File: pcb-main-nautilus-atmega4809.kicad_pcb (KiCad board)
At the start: 4 copper layers, 68.6 x 53.3 mm, 91 parts, among them J1 694106301002, J2 105017-0001, J3 FTSH-105-01-L-DV-007-K, J4 75844-101-06LF, J5 66951-006LF, J6 66951-010LF, J7 66951-008LF, J8 66951-008LF, Q1 BSS138PW, Q2 BSS138PW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

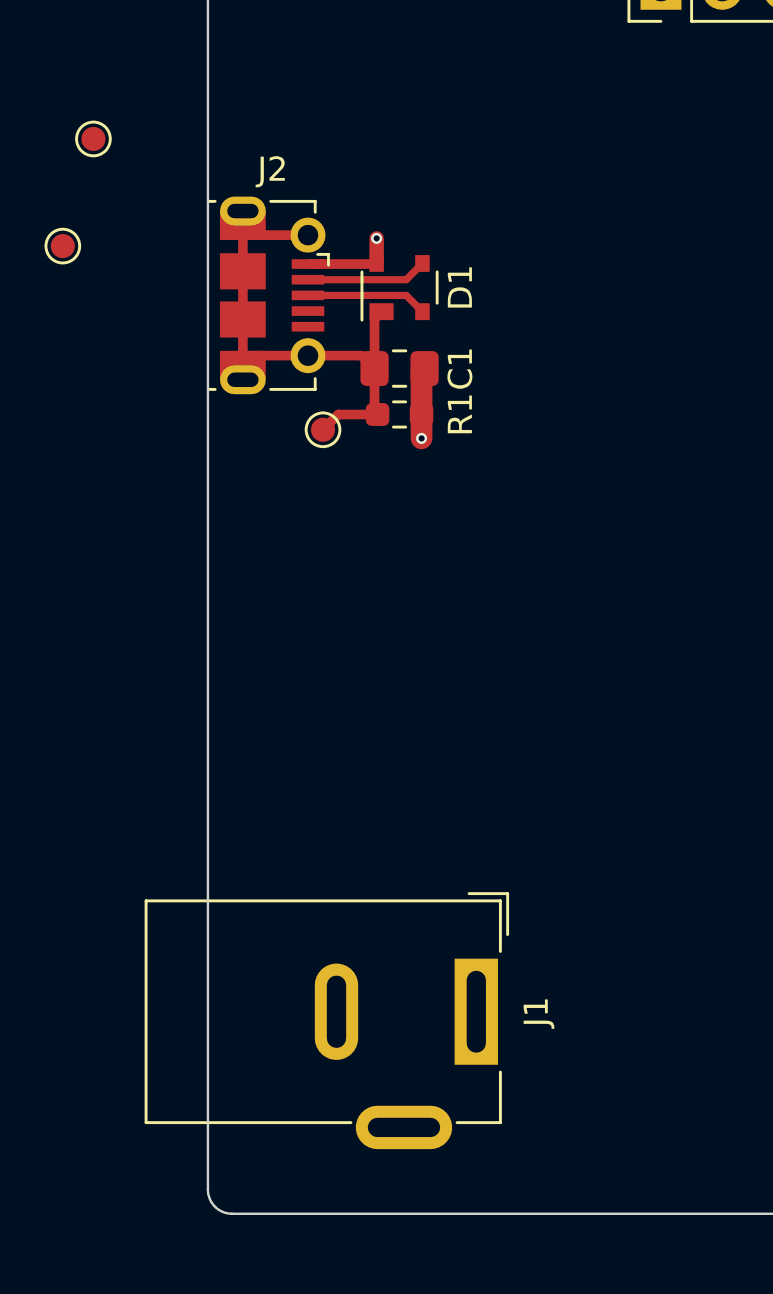
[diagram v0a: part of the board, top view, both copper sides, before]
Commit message: Adjust connector placement to avoid silk DRC errors
Supports #4.
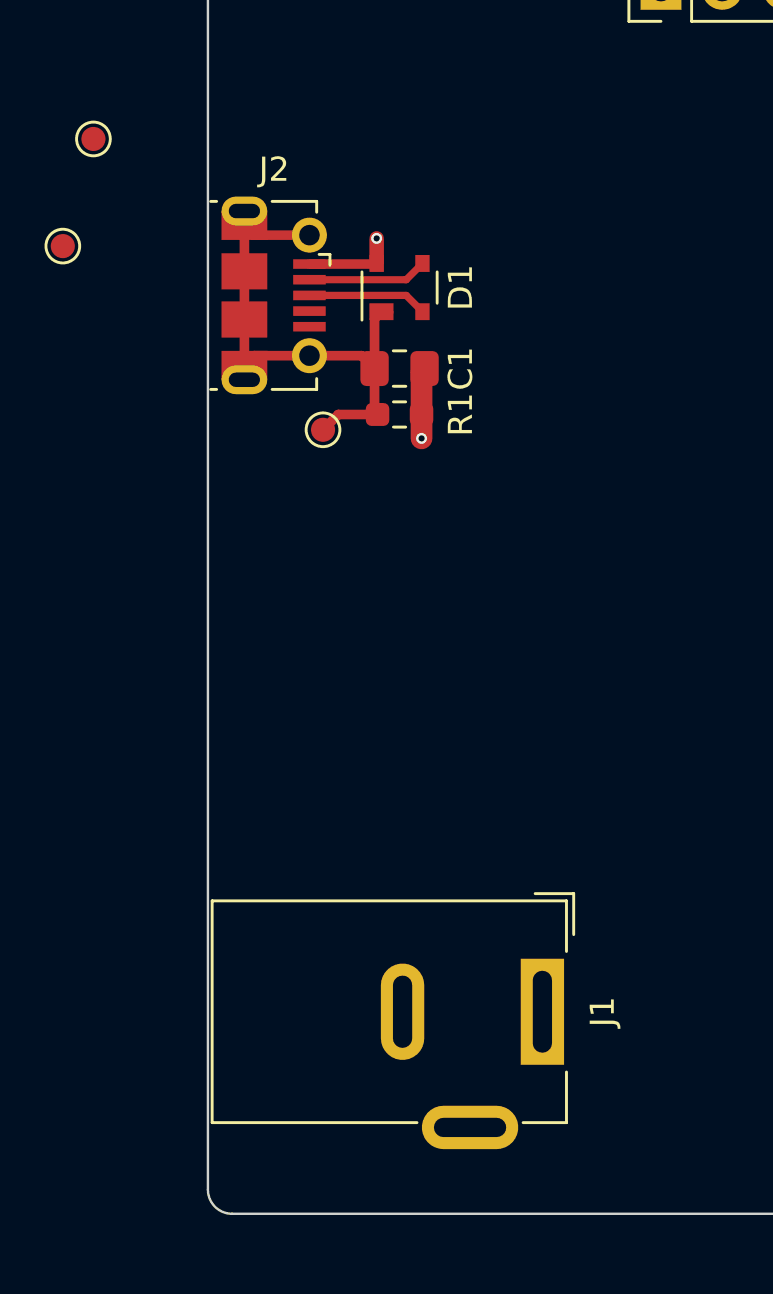
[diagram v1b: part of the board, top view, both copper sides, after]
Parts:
- moved J1 2.74 mm to (113.9, 141.6)
- moved J2 0.06 mm to (102.8, 111.9)
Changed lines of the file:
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@@
   )
   (footprint "Connector_USB:USB_Micro-B_Molex-105017-0001" locked (layer "F.Cu")
-    (at 102.689204 111.9 -90)
+    (at 102.75 111.9 -90)
     (descr "http://www.molex.com/pdm_docs/sd/1050170001_sd.pdf")
     (tags "Micro-USB SMD Typ-B")
@@
   )
   (footprint "Connector_BarrelJack:BarrelJack_Wuerth_6941xx301002" locked (layer "F.Cu")
-    (at 111.134 141.618 -90)
+    (at 113.875 141.618 -90)
     (descr "Wuerth electronics barrel jack connector (5.5mm outher diameter, inner diameter 2.05mm or 2.55mm depending on exact order number), See: http://katalog.we-online.de/em/datasheet/6941xx301002.pdf")
     (tags "connector barrel jack")
@@
   (gr_line locked (start 168.58 144.92) (end 168.58 112.154) (layer "Edge.Cuts") (width 0.1))
   (gr_arc locked (start 100 97.66) (mid 100.292893 96.952893) (end 101 96.66) (layer "Edge.Cuts") (width 0.1))
-  (segment (start 101.851704 109.4) (end 101.451704 109) (width 0.4) (layer "F.Cu") (net 1))
   (segment (start 106.9125 112.8625) (end 107.2 112.575) (width 0.4) (layer "F.Cu") (net 1))
   (segment (start 107.0375 116.84) (end 105.41 116.84) (width 0.4) (layer "F.Cu") (net 1))
-  (segment (start 101.451704 108.4) (end 101.451704 109) (width 0.4) (layer "F.Cu") (net 1))
-  (segment (start 101.451704 114.8) (end 101.451704 115.4) (width 0.4) (layer "F.Cu") (net 1))
-  (segment (start 101.451704 110.9) (end 101.451704 112.9) (width 0.4) (layer "F.Cu") (net 1))
-  (segment (start 104.151704 109.4) (end 101.851704 109.4) (width 0.4) (layer "F.Cu") (net 1))
+  (segment (start 101.5125 108.4) (end 101.5125 109) (width 0.4) (layer "F.Cu") (net 1))
+  (segment (start 101.9125 109.4) (end 101.5125 109) (width 0.4) (layer "F.Cu") (net 1))
+  (segment (start 101.5125 114.8) (end 101.5125 115.4) (width 0.4) (layer "F.Cu") (net 1))
+  (segment (start 101.5125 110.9) (end 101.5125 112.9) (width 0.4) (layer "F.Cu") (net 1))
+  (segment (start 104.2125 114.4) (end 101.9125 114.4) (width 0.4) (layer "F.Cu") (net 1))
   (segment (start 106.9125 116.715) (end 107.0375 116.84) (width 0.4) (layer "F.Cu") (net 1))
   (segment (start 107.635 112.625) (end 107.635 112.575) (width 0.127) (layer "F.Cu") (net 1))
   (segment (start 105.41 116.84) (end 104.775 117.475) (width 0.4) (layer "F.Cu") (net 1))
   (segment (start 106.9125 114.935) (end 106.9125 116.715) (width 0.4) (layer "F.Cu") (net 1))
-  (segment (start 104.151704 114.4) (end 101.851704 114.4) (width 0.4) (layer "F.Cu") (net 1))
+  (segment (start 104.2125 109.4) (end 101.9125 109.4) (width 0.4) (layer "F.Cu") (net 1))
   (segment (start 106.3775 114.4) (end 106.9125 114.935) (width 0.4) (layer "F.Cu") (net 1))
-  (segment (start 101.451704 112.9) (end 101.451704 114.8) (width 0.4) (layer "F.Cu") (net 1))
+  (segment (start 101.5125 112.9) (end 101.5125 114.8) (width 0.4) (layer "F.Cu") (net 1))
   (segment (start 106.9125 114.935) (end 106.9125 112.8625) (width 0.4) (layer "F.Cu") (net 1))
-  (segment (start 104.151704 114.4) (end 106.3775 114.4) (width 0.4) (layer "F.Cu") (net 1))
-  (segment (start 101.851704 114.4) (end 101.451704 114.8) (width 0.4) (layer "F.Cu") (net 1))
-  (segment (start 101.451704 109) (end 101.451704 110.9) (width 0.4) (layer "F.Cu") (net 1))
+  (segment (start 101.5125 109) (end 101.5125 110.9) (width 0.4) (layer "F.Cu") (net 1))
+  (segment (start 104.2125 114.4) (end 106.3775 114.4) (width 0.4) (layer "F.Cu") (net 1))
+  (segment (start 101.9125 114.4) (end 101.5125 114.8) (width 0.4) (layer "F.Cu") (net 1))
   (segment (start 196.6 91.0875) (end 196.6 89.5125) (width 0.3) (layer "F.Cu") (net 2))
   (segment (start 196.6 89.5125) (end 195.9875 88.9) (width 0.3) (layer "F.Cu") (net 2))
@@
   (segment (start 141.605 68.58) (end 141.605 70.485) (width 0.95) (layer "F.Cu") (net 6))
   (segment (start 108.225 111.25) (end 108.9 110.575) (width 0.3) (layer "F.Cu") (net 9))
-  (segment (start 104.151704 111.25) (end 108.225 111.25) (width 0.3) (layer "F.Cu") (net 9))
-  (segment (start 104.151704 111.9) (end 108.225 111.9) (width 0.3) (layer "F.Cu") (net 10))
+  (segment (start 108.225 111.25) (end 104.2125 111.25) (width 0.3) (layer "F.Cu") (net 9))
+  (segment (start 108.225 111.9) (end 104.2125 111.9) (width 0.3) (layer "F.Cu") (net 10))
   (segment (start 108.225 111.9) (end 108.9 112.575) (width 0.3) (layer "F.Cu") (net 10))
-  (segment (start 104.151704 110.6) (end 106.975 110.6) (width 0.4) (layer "F.Cu") (net 11))
   (segment (start 107 110.575) (end 107 109.535) (width 0.6) (layer "F.Cu") (net 11))
   (segment (start 106.975 110.6) (end 107 110.575) (width 0.4) (layer "F.Cu") (net 11))
+  (segment (start 104.2125 110.6) (end 106.975 110.6) (width 0.4) (layer "F.Cu") (net 11))
   (via (at 107 109.535) (size 0.4572) (drill 0.254) (layers "F.Cu" "B.Cu") (net 11))
   (segment (start 65.405 107.315) (end 66.3975 107.315) (width 0.95) (layer "F.Cu") (net 13))

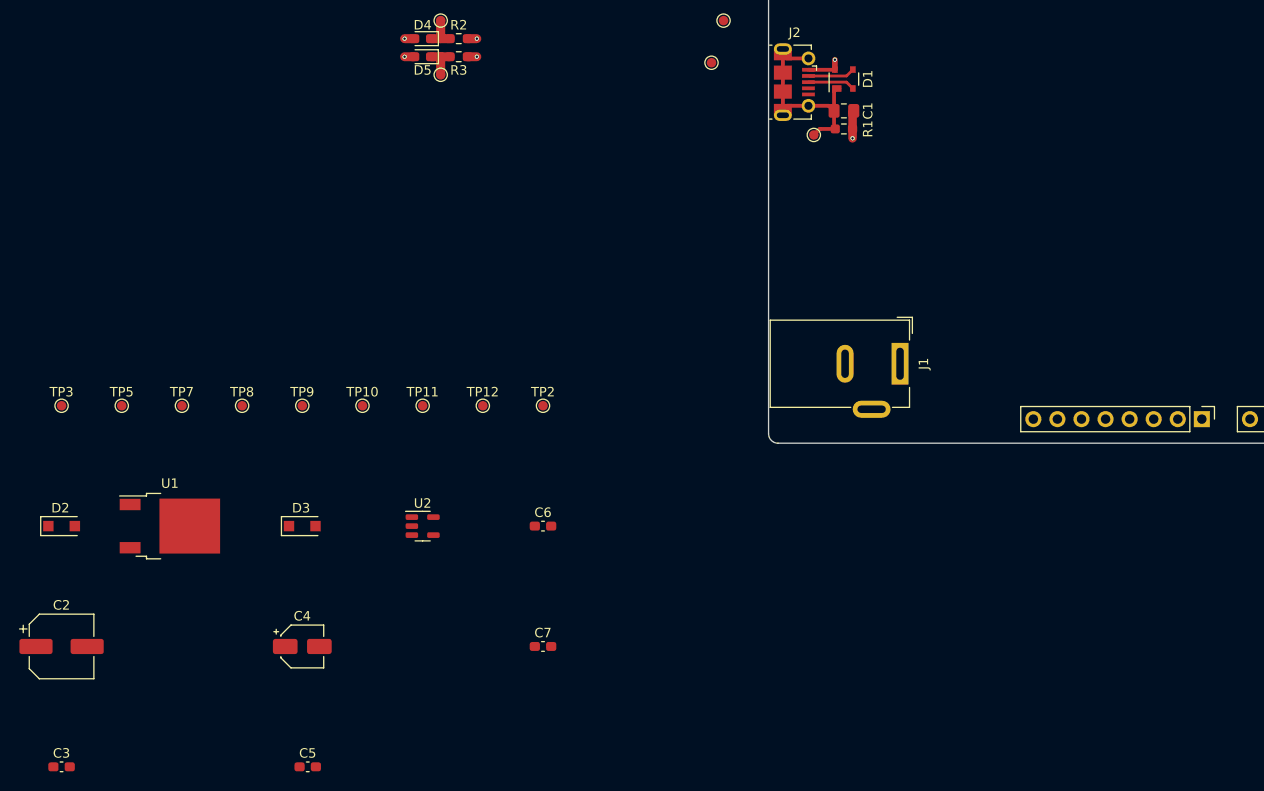
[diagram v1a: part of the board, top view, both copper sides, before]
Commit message: Place 5 V power circuitry
Supports #4.
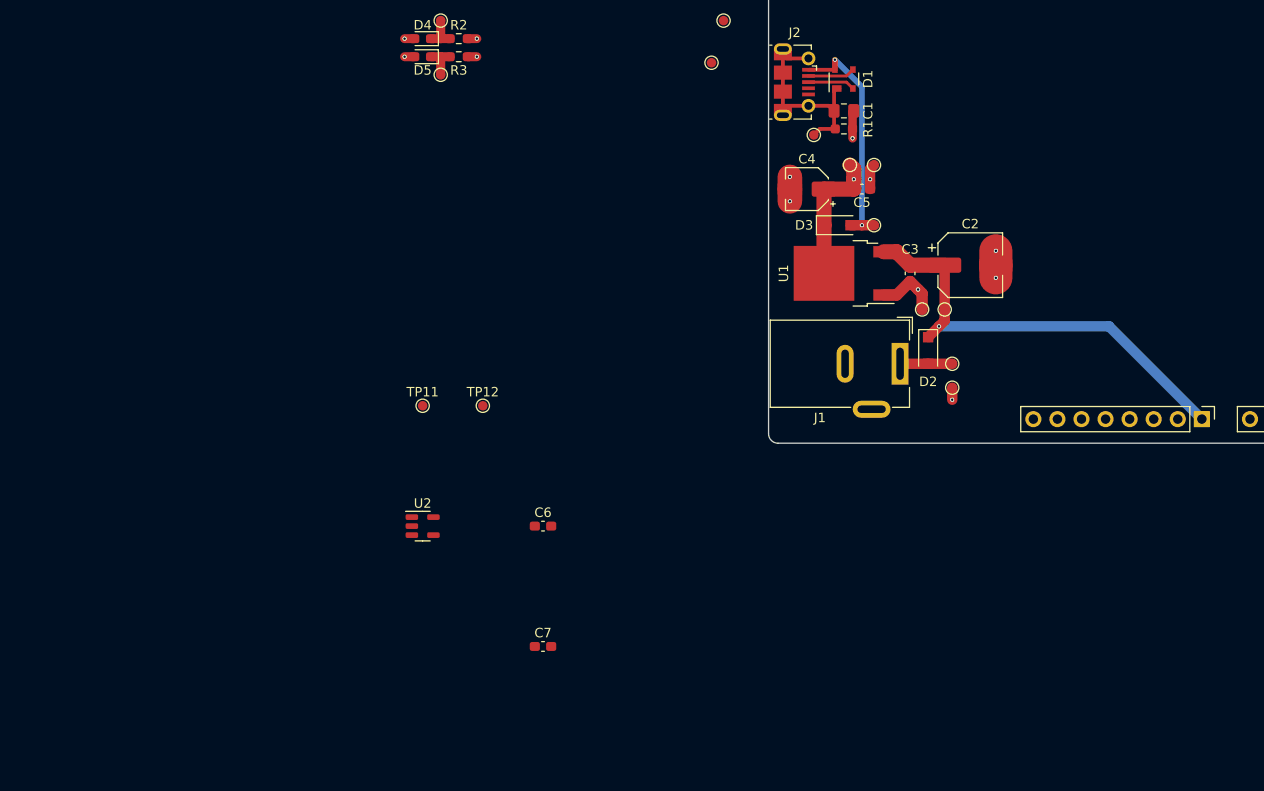
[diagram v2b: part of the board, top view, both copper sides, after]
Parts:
- moved C2 104.0 mm to (121.3, 131.2)
- moved C3 103.6 mm to (114.9, 132.1), turned to -90 degrees
- moved TP3 94.0 mm to (119.4, 144.1)
- moved D2 93.3 mm to (116.8, 140.2), turned to -90 degrees
- moved TP5 87.7 mm to (119.4, 141.6)
- moved C5 84.5 mm to (109.9, 123.2)
- moved TP7 81.1 mm to (118.6, 135.9)
- moved U1 76.0 mm to (108.0, 132.1), turned to 180 degrees
- moved TP8 72.5 mm to (116.2, 135.9)
- moved C4 71.9 mm to (104.0, 123.2), turned to 180 degrees
- moved D3 64.8 mm to (107.2, 127.0)
- moved TP9 63.1 mm to (108.6, 120.7)
- moved TP10 59.7 mm to (111.1, 120.7)
- moved TP2 39.8 mm to (111.1, 127.0)
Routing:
- net /VIN: track 0.00 -> 47.1 mm, vias 0 -> 1
- net /POWER/USB_VBUS: track 3.84 -> 25.0 mm, vias 1 -> 2
- net /GND: track 29.7 -> 45.9 mm, vias 12 -> 19
- net /5V: track 18.9 -> 33.6 mm, vias 10 -> 11
- net /POWER/PWRIN: track 0.00 -> 5.50 mm

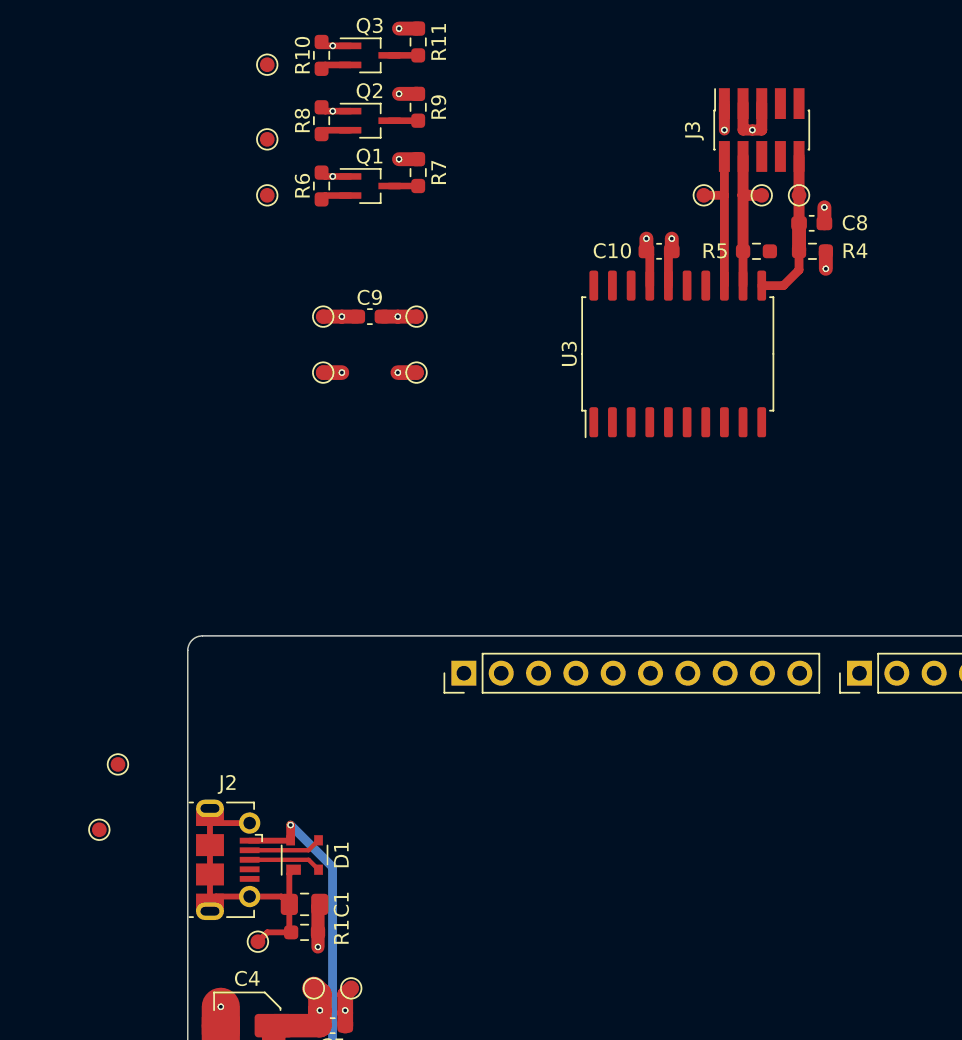
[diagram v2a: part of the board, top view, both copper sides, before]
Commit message: Place UPDI programmer and USB-serial bridge circuitry
Supports #4.
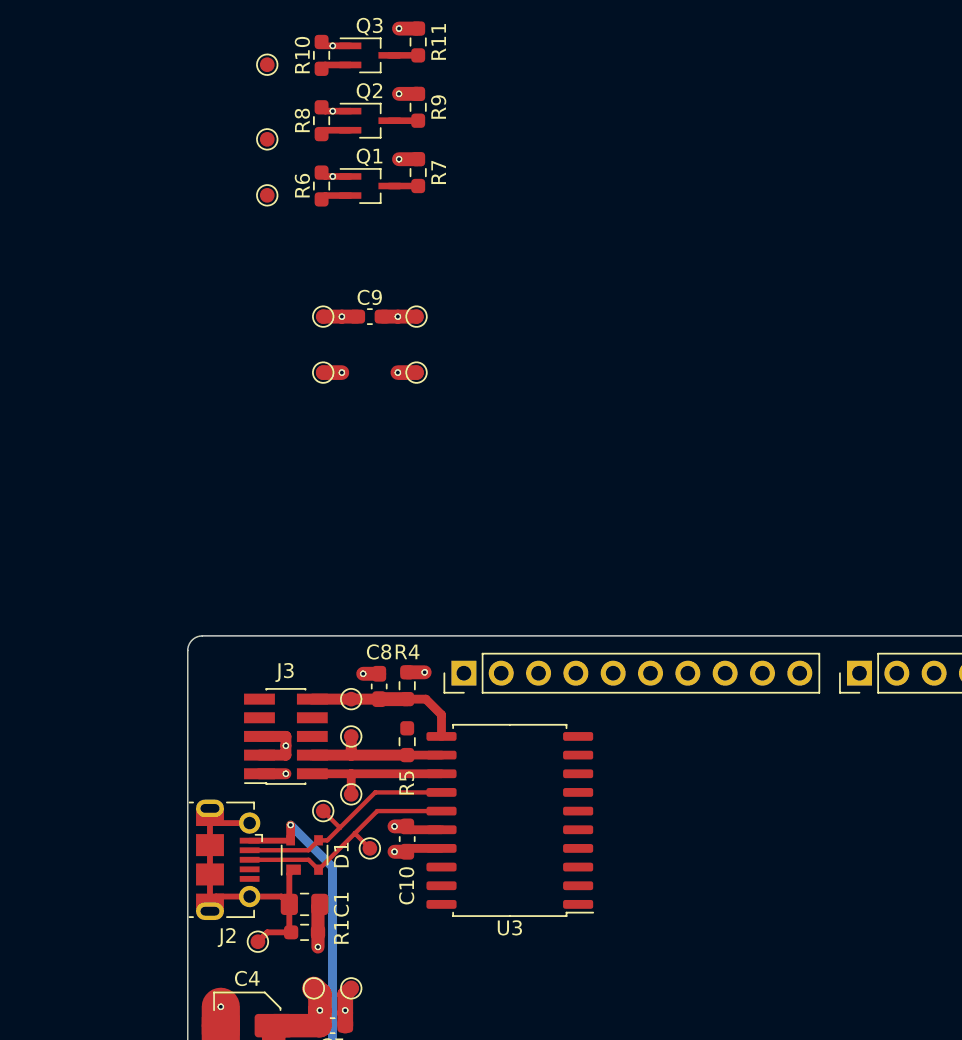
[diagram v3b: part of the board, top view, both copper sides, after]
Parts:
- moved J3 52.5 mm to (106.7, 103.5), turned to 180 degrees
- moved TP15 47.3 mm to (111.1, 107.4), turned to 180 degrees
- moved TP14 46.2 mm to (111.1, 103.5), turned to 180 degrees
- moved TP13 45.9 mm to (111.1, 101.0), turned to 180 degrees
- moved C10 43.5 mm to (114.9, 110.5), turned to 90 degrees
- moved C8 43.1 mm to (113.0, 100.1), turned to -90 degrees
- moved R5 41.0 mm to (114.9, 103.9), turned to -90 degrees
- moved R4 40.4 mm to (114.9, 100.1), turned to -90 degrees
- moved U3 33.7 mm to (121.9, 109.2), turned to 180 degrees
- moved TP4 18.5 mm to (112.4, 111.1)
- moved TP6 14.3 mm to (109.2, 108.6)
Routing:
- net /UPDI PROGRAMMER AND USB-SERIAL BRIDGE/USB_D+: track 4.97 -> 16.4 mm
- net /UPDI PROGRAMMER AND USB-SERIAL BRIDGE/USB_D-: track 4.97 -> 16.3 mm

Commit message: Finish place and route
Supports #4.
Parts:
- moved TP23 81.9 mm to (147.5, 122.0)
- moved TP24 80.8 mm to (149.8, 122.0)
- moved TP21 76.8 mm to (137.2, 123.0)
- moved TP20 76.5 mm to (133.0, 123.0)
- moved TP22 74.8 mm to (130.0, 125.2)
- moved R15 74.7 mm to (134.8, 131.1)
- moved R16 74.7 mm to (134.8, 133.0)
- moved TP32 74.7 mm to (132.2, 129.2)
- moved TP33 74.7 mm to (132.2, 134.9)
- moved D7 74.7 mm to (129.7, 131.1)
- moved D8 74.7 mm to (129.7, 133.0)
- moved TP31 69.8 mm to (128.0, 121.8), turned to -90 degrees
- moved R11 69.2 mm to (139.4, 121.3), turned to 180 degrees
- moved D6 68.7 mm to (126.0, 119.8), turned to 90 degrees
- moved SW1 67.5 mm to (162.2, 136.2), turned to -90 degrees
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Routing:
- net /MCU/D19/A5/SCL: track 0.00 -> 98.1 mm, vias 0 -> 1
- net /MCU/D18/A4/SDA: track 0.00 -> 98.0 mm, vias 0 -> 1
- net /MCU/D13/SCK: track 1.03 -> 83.9 mm
- net /MCU/AREF: track 0.00 -> 74.4 mm, vias 0 -> 1
- net /3.3V: track 15.8 -> 83.7 mm, vias 8 -> 11
- net /MCU/D5: track 0.00 -> 59.4 mm, vias 0 -> 1
- net /MCU/D11/COPI: track 0.00 -> 59.2 mm, vias 0 -> 1
- net /MCU/D2: track 0.00 -> 58.6 mm, vias 0 -> 1
- net /MCU/D12/CIPO: track 0.00 -> 58.0 mm, vias 0 -> 1
- net /MCU/D6: track 0.00 -> 57.9 mm, vias 0 -> 1
- net /MCU/D3: track 0.00 -> 57.4 mm, vias 0 -> 1
- net /MCU/D0/RX: track 0.00 -> 56.0 mm, vias 0 -> 1
- net /MCU/D1/TX: track 0.00 -> 55.2 mm, vias 0 -> 1
- net /MCU/D4: track 0.00 -> 55.0 mm, vias 0 -> 1
- net /MCU/D8: track 0.00 -> 50.8 mm, vias 0 -> 1
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- added copper zone on B.Cu, net /3.3V

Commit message: Add header pin labels
Supports #4.
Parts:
- moved C11 6.13 mm to (161.2, 142.0), turned to 0 degrees
- moved R13 5.20 mm to (161.2, 140.2), turned to 180 degrees
- moved R12 4.91 mm to (161.2, 138.5), turned to 180 degrees
- moved TP30 4.12 mm to (164.8, 138.5)
- moved SW1 3.95 mm to (161.0, 132.5)
- moved C17 2.06 mm to (152.8, 141.0), turned to 180 degrees
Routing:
- net /MCU/~{RESET}: track 47.5 -> 52.2 mm
- net Net-(R12-Pad1): track 13.3 -> 15.3 mm
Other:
- board text added: "3.3V"
- board text added: "5V"
- board text added: "A0"
- board text added: "A1"
- board text added: "A2"
- board text added: "A3"
- board text added: "A4"
- board text added: "A5"
- board text added: "D0"
- board text added: "D1"
- board text added: "D10"
- board text added: "D11"
- board text added: "D12"
- board text added: "D13"
- board text added: "D2"
- board text added: "D3"
- board text added: "D4"
- board text added: "D5"
- board text added: "D6"
- board text added: "D7"
- board text added: "D8"
- board text added: "D9"
- board text added: "GND"
- board text added: "IOREF"
- board text added: "VIN"
- board text added: "~{RESET}"
